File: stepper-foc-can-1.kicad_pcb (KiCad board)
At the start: 4 copper layers, 42 x 48 mm, 87 parts, among them J1 TC2030, J2 Conn_01x02, J3 Conn_01x04_Pin, J4 Conn_01x02, J5 Conn_01x02, M1 Stepper_Motor_bipolar, SW1 SW_Push, SW2 SW_Push, SW3 SW_Push, SW4 SW_Push, U1 STM32G474RBTx, U2 MX25947, U3 TPS62933, U4 TCAN3413, U5 AS5047P, U6 DRV8874, U7 INA241A3IDDF, U8 DRV8874, U9 INA241A3IDDF, Y1 Crystal_GND24

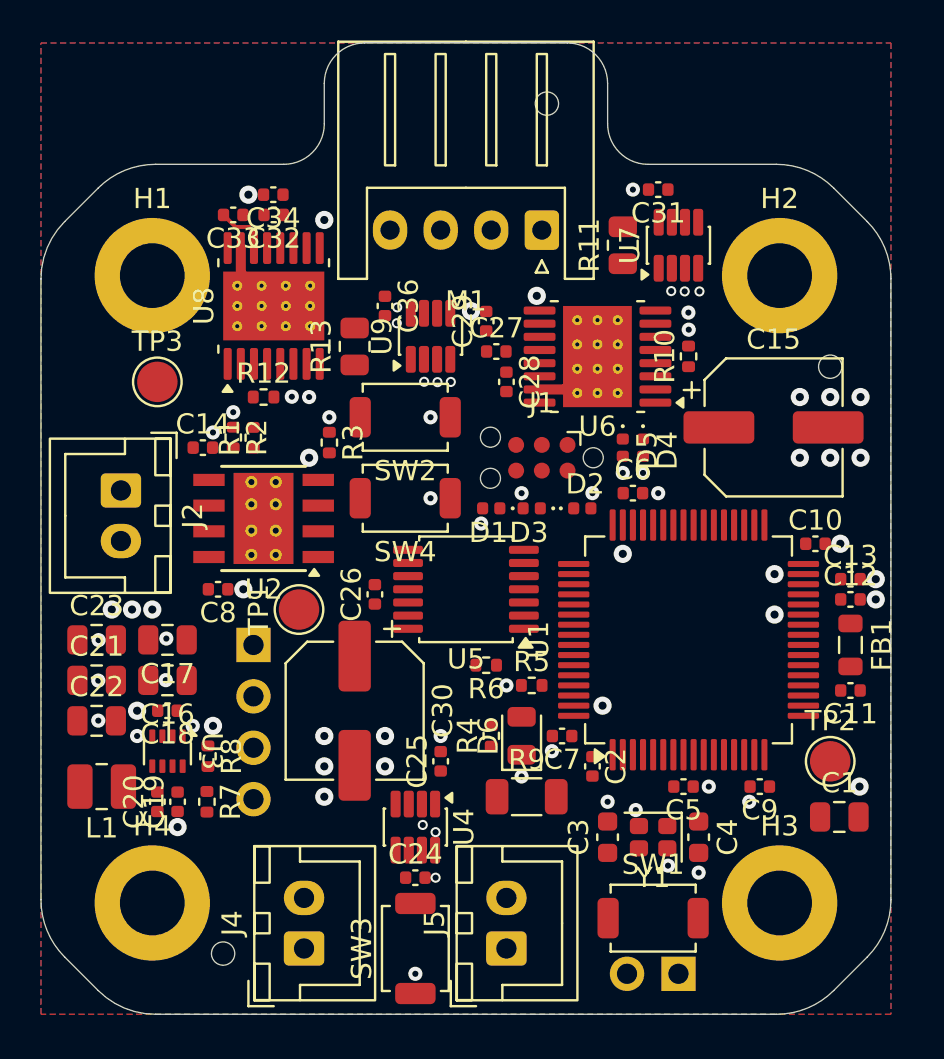
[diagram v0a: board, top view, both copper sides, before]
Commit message: schem: reorganize programmable gpios
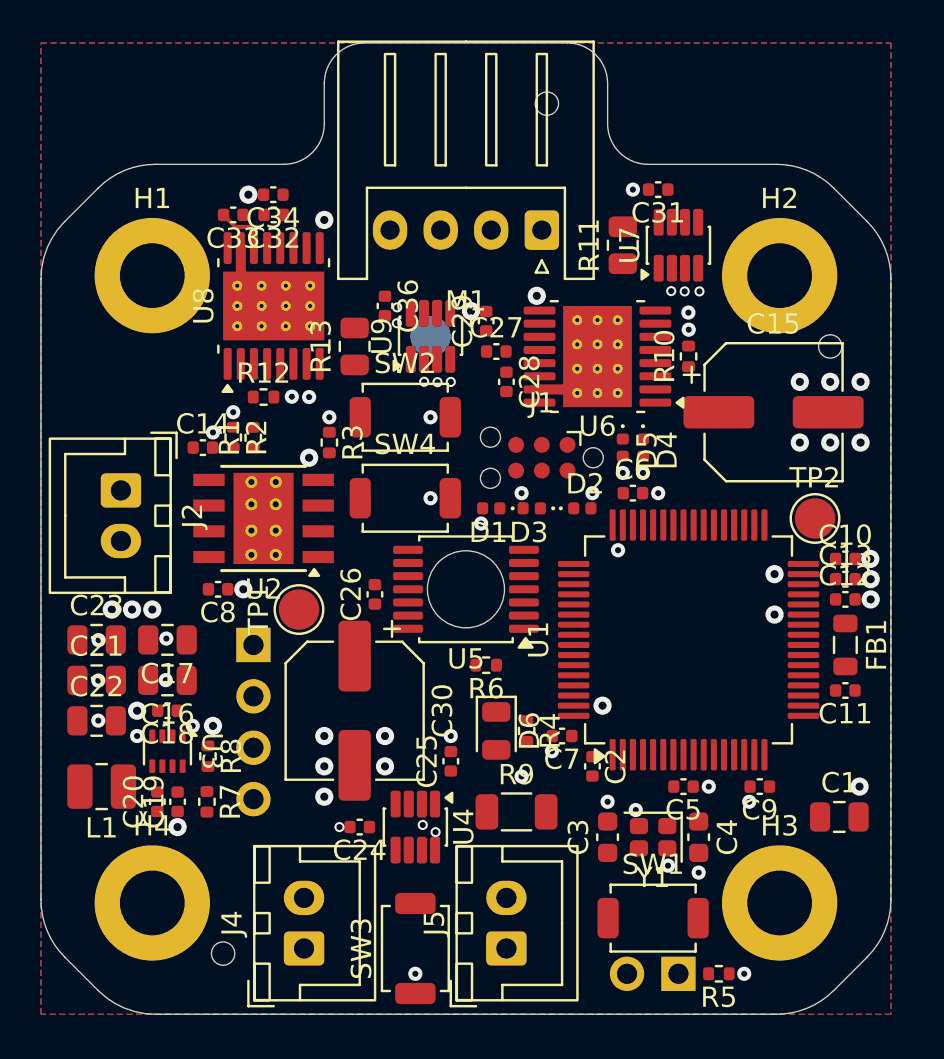
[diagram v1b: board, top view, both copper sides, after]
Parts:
- TP3: moved to B.Cu
- moved R5 17.0 mm to (156.5, 100.0), turned to 180 degrees
- moved TP3 13.7 mm to (142.2, 68.5), turned to 180 degrees
- moved TP2 12.0 mm to (161.2, 77.5)
- moved C24 3.72 mm to (138.8, 92.8), turned to 180 degrees
- moved R4 1.77 mm to (147.0, 88.0), turned to -90 degrees
- moved C10 1.66 mm to (162.8, 79.5)
- moved D6 1.27 mm to (145.5, 88.0), turned to -90 degrees
- moved H5 1.00 mm to (162.0, 69.0)
- moved R9 0.90 mm to (146.5, 92.0)
- moved C15 0.75 mm to (159.2, 72.2)
- moved C25 0.50 mm to (143.2, 89.5)
- moved C11 0.25 mm to (162.8, 86.0)
- moved C12 0.25 mm to (162.8, 81.5)
- moved C13 0.25 mm to (162.8, 80.5)
- moved FB1 0.25 mm to (162.8, 83.8)
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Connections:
- R4 pad 1: Net-(U1-PB15) -> Net-(U1-PB9)
- SW4 pad 2: /BTN1 -> /BTN2
- U1 pad 10: /IN1_B -> unconnected-(U1-PC2-Pad10)
- U1 pad 11: /IN2_B -> unconnected-(U1-PC3-Pad11)
- U1 pad 18: /SPI_CS -> unconnected-(U1-PA4-Pad18)
- U1 pad 19: /SPI_CLK -> unconnected-(U1-PA5-Pad19)
- U1 pad 2: /~{FAULT_A} -> unconnected-(U1-PC13-Pad2)
- U1 pad 20: /SPI_MISO -> unconnected-(U1-PA6-Pad20)
- U1 pad 21: /SPI_MOSI -> unconnected-(U1-PA7-Pad21)
- U1 pad 24: /SNS_A -> unconnected-(U1-PB0-Pad24)
- U1 pad 25: /SNS_B -> unconnected-(U1-PB1-Pad25)
- U1 pad 3: /~{SLEEP_B} -> unconnected-(U1-PC14-Pad3)
- U1 pad 33: unconnected-(U1-PB11-Pad33) -> /SNS_A
- U1 pad 34: unconnected-(U1-PB12-Pad34) -> /SNS_B
- U1 pad 35: unconnected-(U1-PB13-Pad35) -> /BTN1
- U1 pad 36: unconnected-(U1-PB14-Pad36) -> /~{FAULT_A}
- U1 pad 37: Net-(U1-PB15) -> /~{SLEEP_A}
- U1 pad 38: unconnected-(U1-PC6-Pad38) -> /IN2_A
- U1 pad 39: unconnected-(U1-PC7-Pad39) -> /IN1_A
- U1 pad 4: /~{FAULT_B} -> unconnected-(U1-PC15-Pad4)
- U1 pad 40: unconnected-(U1-PC8-Pad40) -> /IN2_B
- U1 pad 41: unconnected-(U1-PC9-Pad41) -> /IN1_B
- U1 pad 42: /ENC_A -> /~{SLEEP_B}
- U1 pad 43: /ENC_B -> /~{FAULT_B}
- U1 pad 44: /ENC_I -> /BTN2
- U1 pad 45: /CAN_RX -> /ENC_B
- U1 pad 46: /CAN_TX -> /ENC_A
- U1 pad 51: unconnected-(U1-PA15-Pad51) -> /SPI_CS
- U1 pad 52: unconnected-(U1-PC10-Pad52) -> /SPI_CLK
- U1 pad 53: unconnected-(U1-PC11-Pad53) -> /SPI_MISO
- U1 pad 54: /~{SLEEP_A} -> /SPI_MOSI
- U1 pad 57: unconnected-(U1-PB4-Pad57) -> /ENC_I
- U1 pad 58: /BTN1 -> /CAN_RX
- U1 pad 59: unconnected-(U1-PB6-Pad59) -> /CAN_TX
- U1 pad 62: unconnected-(U1-PB9-Pad62) -> Net-(U1-PB9)
- U1 pad 8: /IN1_A -> unconnected-(U1-PC0-Pad8)
- U1 pad 9: /IN2_A -> unconnected-(U1-PC1-Pad9)
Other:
- outline, holes or cut-outs redrawn

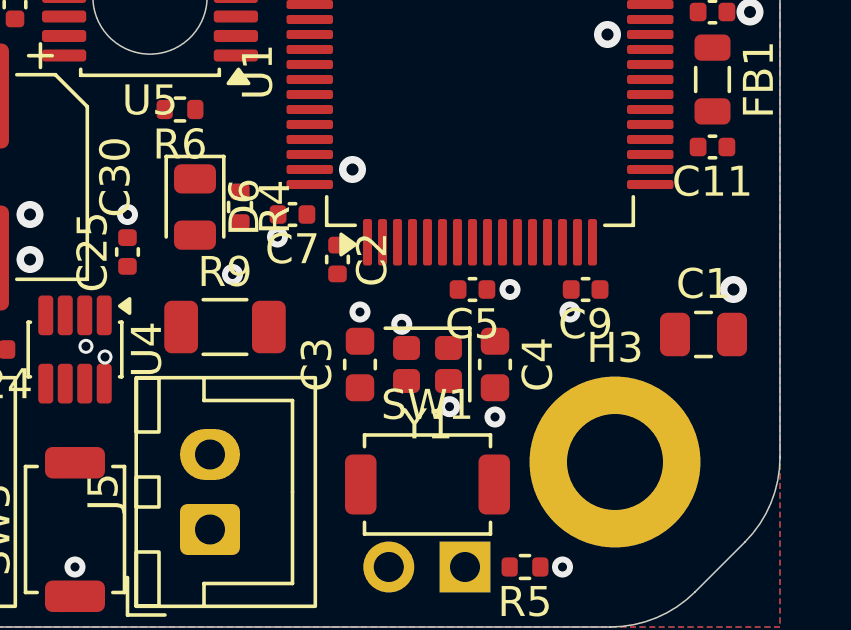
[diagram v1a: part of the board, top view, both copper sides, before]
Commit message: pcb: add xtal routing
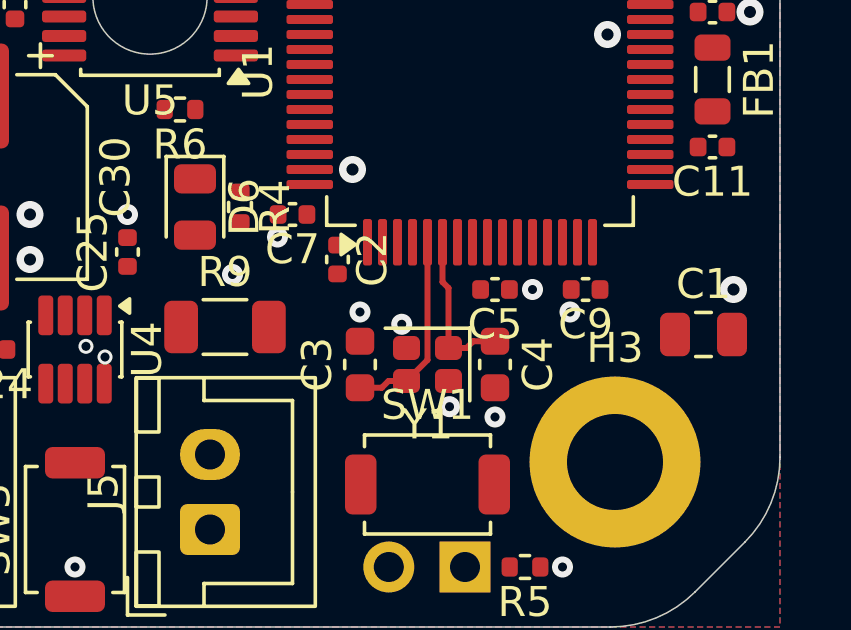
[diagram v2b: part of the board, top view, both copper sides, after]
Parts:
- moved C5 0.75 mm to (155.5, 90.8)
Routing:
- net /XTAL_I: track 0.00 -> 6.56 mm
- net /XTAL_O: track 0.00 -> 5.25 mm
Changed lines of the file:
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@@
 	(footprint "Capacitor_SMD:C_0402_1005Metric"
 		(layer "F.Cu")
-		(at 154.75 90.75 180)
+		(at 155.5 90.75 180)
 		(descr "Capacitor SMD 0402 (1005 Metric), square (rectangular) end terminal, IPC-7351 nominal, (Body size source: IPC-SM-782 page 76, https://www.pcb-3d.com/wordpress/wp-content/uploads/ipc-sm-782a_amendment_1_and_2.pdf)")
 		(tags "capacitor")
@@
 	)
 	(via
-		(at 156 90.75)
+		(at 156.75 90.75)
 		(size 0.7)
 		(drill 0.3)
@@
 	)
 	(segment
+		(start 153.95 92.7)
+		(end 154.55 92.7)
+		(width 0.2)
+		(layer "F.Cu")
+		(net "/XTAL_O")
+	)
+	(segment
+		(start 154.775 92.475)
+		(end 155.5 92.475)
+		(width 0.2)
+		(layer "F.Cu")
+		(net "/XTAL_O")
+	)
+	(segment
+		(start 153.95 90.7)
+		(end 153.75 90.5)
+		(width 0.2)
+		(layer "F.Cu")
+		(net "/XTAL_O")
+	)
+	(segment
+		(start 153.75 90.5)
+		(end 153.75 89.175)
+		(width 0.2)
+		(layer "F.Cu")
+		(net "/XTAL_O")
+	)
+	(segment
+		(start 153.95 92.7)
+		(end 153.95 90.7)
+		(width 0.2)
+		(layer "F.Cu")
+		(net "/XTAL_O")
+	)
+	(segment
+		(start 154.55 92.7)
+		(end 154.775 92.475)
+		(width 0.2)
+		(layer "F.Cu")
+		(net "/XTAL_O")
+	)
+	(segment
+		(start 153.25 93.1)
+		(end 152.55 93.8)
+		(width 0.2)
+		(layer "F.Cu")
+		(net "/XTAL_I")
+	)
+	(segment
+		(start 153.25 89.175)
+		(end 153.25 93.1)
+		(width 0.2)
+		(layer "F.Cu")
+		(net "/XTAL_I")
+	)
+	(segment
+		(start 151.95 93.8)
+		(end 151.725 94.025)
+		(width 0.2)
+		(layer "F.Cu")
+		(net "/XTAL_I")
+	)
+	(segment
+		(start 151.725 94.025)
+		(end 151 94.025)
+		(width 0.2)
+		(layer "F.Cu")
+		(net "/XTAL_I")
+	)
+	(segment
+		(start 152.55 93.8)
+		(end 151.95 93.8)
+		(width 0.2)
+		(layer "F.Cu")
+		(net "/XTAL_I")
+	)
+	(segment
 		(start 133.525 64.1375)
 		(end 133.525 63.350001)
@@
 	)
 	(zone
+		(layer "F.Cu")
+		(hatch edge 0.5)
+		(connect_pads
+			(clearance 0)
+		)
+		(min_thickness 0.25)
+		(keepout
+			(tracks allowed)
+			(vias allowed)
+			(pads allowed)
+			(copperpour not_allowed)
+			(footprints allowed)
+		)
+		(placement
+			(enabled no)
+			(sheetname "/")
+		)
+		(fill
+			(thermal_gap 0.5)
+			(thermal_bridge_width 0.5)
+			(island_removal_mode 0)
+		)
+		(polygon
+			(pts
+				(xy 150.5 94.25) (xy 151 94.75) (xy 155.75 94.75) (xy 156 94.5) (xy 156 92) (xy 155.5 91.5) (xy 151 91.5)
+				(xy 150.5 92)
+			)
+		)
+	)
+	(zone

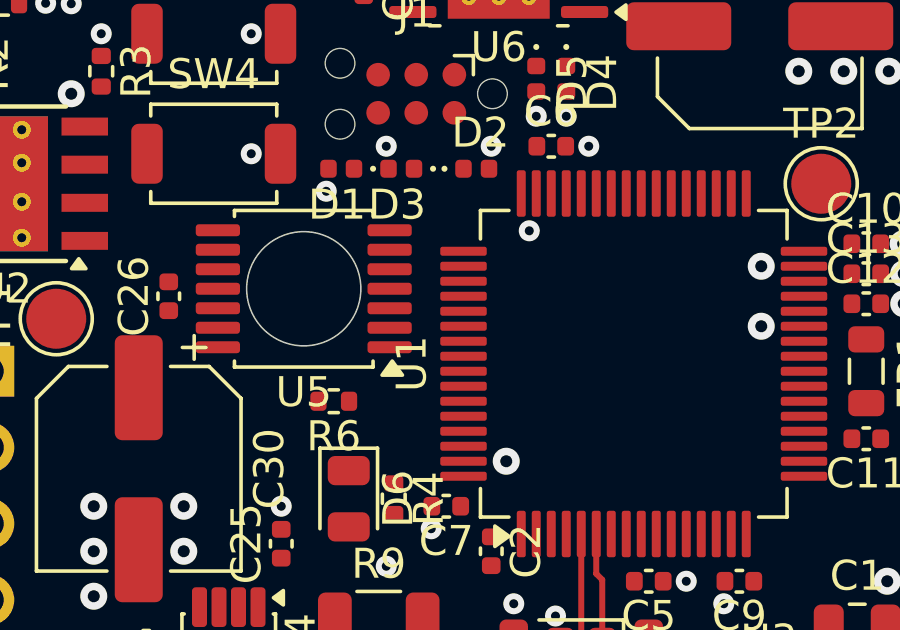
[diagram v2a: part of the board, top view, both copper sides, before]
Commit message: pcb: add SPI routing
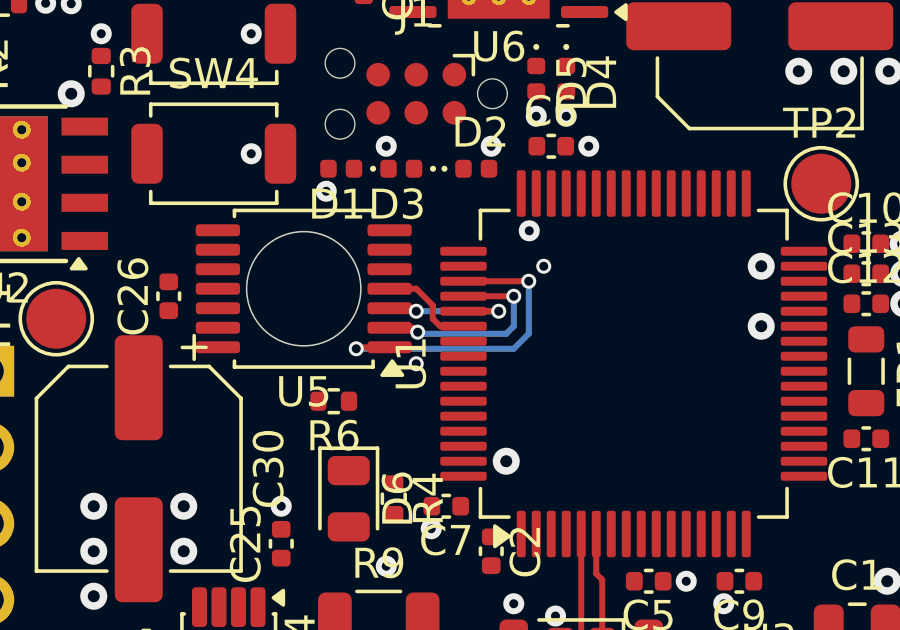
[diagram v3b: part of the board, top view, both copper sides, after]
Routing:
- net /SPI_CS: track 0.00 -> 11.0 mm, vias 0 -> 2
- net /SPI_CLK: track 0.00 -> 7.00 mm, vias 0 -> 2
- net /SPI_MISO: track 0.00 -> 4.85 mm, vias 0 -> 2
- net /SPI_MOSI: track 0.00 -> 3.24 mm
- net GND: vias 76 -> 78
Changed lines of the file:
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@@
+	)
+	(via
+		(at 152 80.25)
+		(size 0.5)
+		(drill 0.3)
+		(layers "F.Cu" "B.Cu")
+		(free yes)
+		(net "GND")
 	)
 	(via
@@
 	)
 	(via
+		(at 147.75 83.5)
+		(size 0.5)
+		(drill 0.3)
+		(layers "F.Cu" "B.Cu")
+		(free yes)
+		(net "GND")
+	)
+	(via
 		(at 163.45 90.75)
 		(size 0.9)
@@
 	)
 	(segment
+		(start 151.5 80.75)
+		(end 149.325 80.75)
+		(width 0.2)
+		(layer "F.Cu")
+		(net "/SPI_CS")
+	)
+	(segment
+		(start 146.8625 82.95)
+		(end 145.8 82.95)
+		(width 0.2)
+		(layer "F.Cu")
+		(net "/SPI_CS")
+	)
+	(segment
+		(start 145.8 82.95)
+		(end 145.75 83)
+		(width 0.2)
+		(layer "F.Cu")
+		(net "/SPI_CS")
+	)
+	(via
+		(at 145.75 83)
+		(size 0.5)
+		(drill 0.3)
+		(layers "F.Cu" "B.Cu")
+		(net "/SPI_CS")
+	)
+	(via
+		(at 151.5 80.75)
+		(size 0.5)
+		(drill 0.3)
+		(layers "F.Cu" "B.Cu")
+		(net "/SPI_CS")
+	)
+	(segment
+		(start 151.5 82.5)
+		(end 151 83)
+		(width 0.2)
+		(layer "B.Cu")
+		(net "/SPI_CS")
+	)
+	(segment
+		(start 151.5 80.75)
+		(end 151.5 82.5)
+		(width 0.2)
+		(layer "B.Cu")
+		(net "/SPI_CS")
+	)
+	(segment
+		(start 151 83)
+		(end 145.75 83)
+		(width 0.2)
+		(layer "B.Cu")
+		(net "/SPI_CS")
+	)
+	(segment
+		(start 146.8625 82.3)
+		(end 147.650239 82.3)
+		(width 0.2)
+		(layer "F.Cu")
+		(net "/SPI_CLK")
+	)
+	(segment
+		(start 147.650239 82.3)
+		(end 147.798129 82.44789)
+		(width 0.2)
+		(layer "F.Cu")
+		(net "/SPI_CLK")
+	)
+	(segment
+		(start 151 81.25)
+		(end 149.325 81.25)
+		(width 0.2)
+		(layer "F.Cu")
+		(net "/SPI_CLK")
+	)
+	(via
+		(at 147.798129 82.44789)
+		(size 0.5)
+		(drill 0.3)
+		(layers "F.Cu" "B.Cu")
+		(net "/SPI_CLK")
+	)
+	(via
+		(at 151 81.25)
+		(size 0.5)
+		(drill 0.3)
+		(layers "F.Cu" "B.Cu")
+		(net "/SPI_CLK")
+	)
+	(segment
+		(start 147.850239 82.5)
+		(end 147.798129 82.44789)
+		(width 0.2)
+		(layer "B.Cu")
+		(net "/SPI_CLK")
+	)
+	(segment
+		(start 151 81.25)
+		(end 151 82.25)
+		(width 0.2)
+		(layer "B.Cu")
+		(net "/SPI_CLK")
+	)
+	(segment
+		(start 150.75 82.5)
+		(end 147.850239 82.5)
+		(width 0.2)
+		(layer "B.Cu")
+		(net "/SPI_CLK")
+	)
+	(segment
+		(start 151 82.25)
+		(end 150.75 82.5)
+		(width 0.2)
+		(layer "B.Cu")
+		(net "/SPI_CLK")
+	)
+	(segment
+		(start 150.5 81.75)
+		(end 149.325 81.75)
+		(width 0.2)
+		(layer "F.Cu")
+		(net "/SPI_MISO")
+	)
+	(segment
+		(start 146.8625 81.65)
+		(end 147.65 81.65)
+		(width 0.2)
+		(layer "F.Cu")
+		(net "/SPI_MISO")
+	)
+	(segment
+		(start 147.65 81.65)
+		(end 147.75 81.75)
+		(width 0.2)
+		(layer "F.Cu")
+		(net "/SPI_MISO")
+	)
+	(via
+		(at 147.75 81.75)
+		(size 0.5)
+		(drill 0.3)
+		(layers "F.Cu" "B.Cu")
+		(net "/SPI_MISO")
+	)
+	(via
+		(at 150.5 81.75)
+		(size 0.5)
+		(drill 0.3)
+		(layers "F.Cu" "B.Cu")
+		(net "/SPI_MISO")
+	)
+	(segment
+		(start 147.75 81.75)
+		(end 150.5 81.75)
+		(width 0.2)
+		(layer "B.Cu")
+		(net "/SPI_MISO")
+	)
+	(segment
+		(start 147.75 81)
+		(end 148.3 81.55)
+		(width 0.2)
+		(layer "F.Cu")
+		(net "/SPI_MOSI")
+	)
+	(segment
+		(start 146.8625 81)
+		(end 147.75 81)
+		(width 0.2)
+		(layer "F.Cu")
+		(net "/SPI_MOSI")
+	)
+	(segment
+		(start 148.3 81.999999)
+		(end 148.550001 82.25)
+		(width 0.2)
+		(layer "F.Cu")
+		(net "/SPI_MOSI")
+	)
+	(segment
+		(start 148.550001 82.25)
+		(end 149.325 82.25)
+		(width 0.2)
+		(layer "F.Cu")
+		(net "/SPI_MOSI")
+	)
+	(segment
+		(start 148.3 81.55)
+		(end 148.3 81.999999)
+		(width 0.2)
+		(layer "F.Cu")
+		(net "/SPI_MOSI")
+	)
+	(segment

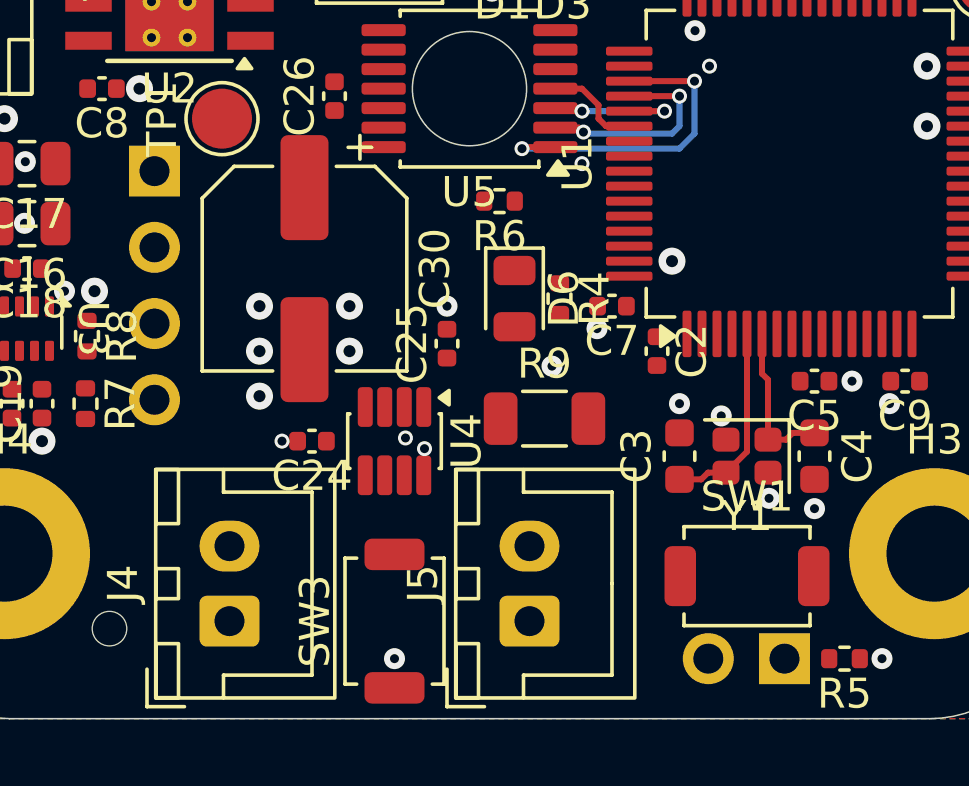
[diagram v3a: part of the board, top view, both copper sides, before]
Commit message: pcb: add can routing
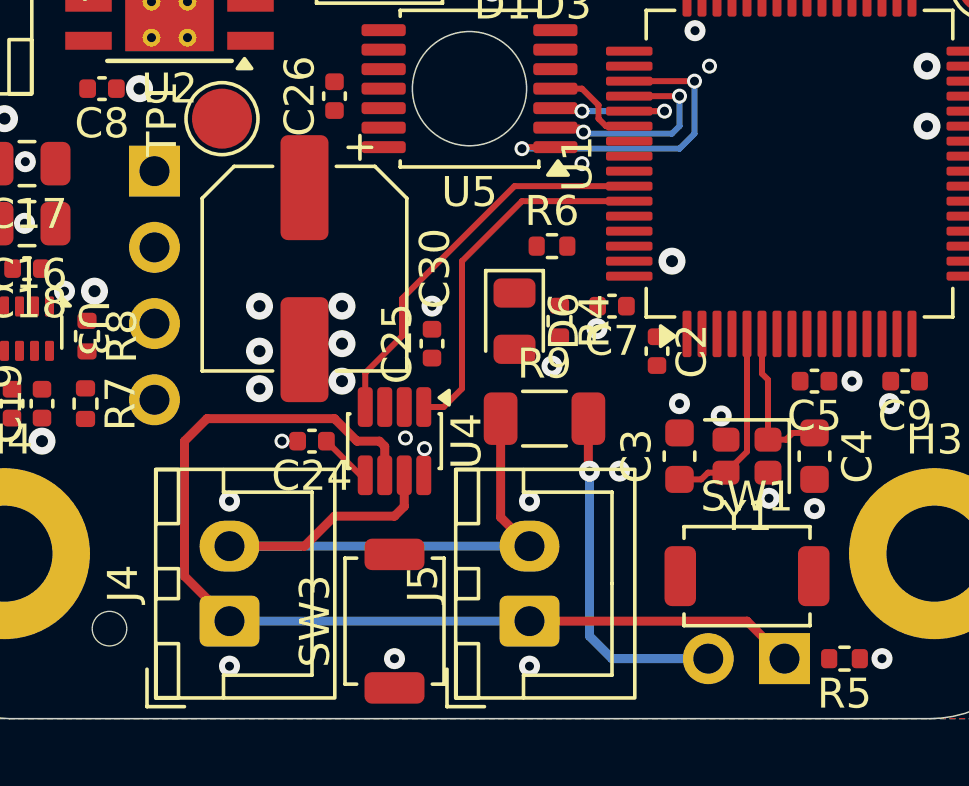
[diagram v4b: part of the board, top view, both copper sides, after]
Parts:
- moved R6 2.30 mm to (146.8, 86.2), turned to 0 degrees
- moved D6 0.75 mm to (145.5, 88.8)
- moved R4 0.75 mm to (147.0, 88.8)
- moved C25 0.50 mm to (142.8, 89.5)
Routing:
- net /CANL: track 0.00 -> 34.0 mm
- net /CANH: track 0.00 -> 22.1 mm
- net /CAN_RX: track 0.00 -> 13.2 mm
- net /CAN_TX: track 0.00 -> 12.2 mm
- net Net-(JP1-B): track 0.00 -> 11.5 mm, vias 0 -> 1
- net +3V3: track 0.00 -> 1.77 mm
- net GND: vias 78 -> 84
